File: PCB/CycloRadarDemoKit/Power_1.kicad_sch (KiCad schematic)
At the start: 33 parts, among them J401 20-16V Supply Voltage, Q401 SI2309CDS, U401 INA3221, U402 RT8259, U403 AP63205WU

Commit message: starting the mockup
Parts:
- J401: footprint (none) -> Connector_Molex:Molex_39521-1002; Mouser (none) -> 538-39521-1002
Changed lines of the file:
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@@
       (effects (font (size 1.27 1.27)))
     )
-    (property "Footprint" "" (at 64.77 113.03 0)
+    (property "Footprint" "Connector_Molex:Molex_39521-1002" (at 64.77 113.03 0)
       (effects (font (size 1.27 1.27)) hide)
     )
@@
       (effects (font (size 1.27 1.27)) hide)
     )
+    (property "Mouser" "538-39521-1002" (at 64.77 113.03 0)
+      (effects (font (size 1.27 1.27)) hide)
+    )

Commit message: layout mockup done
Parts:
- R406: symbol Device:R_Shunt -> Analog:R_Shunt
- R407: footprint Resistor_SMD:R_0805_2012Metric -> Resistor_SMD:R_1210_3225Metric; symbol Device:R_Shunt -> Analog:R_Shunt; LCSC C175747 -> C175910; Power 125mW -> 500mW
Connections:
- net at Q401.3 (S), R406.1: now also R402.2
- net at C405.1, C408.1, R406.2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: now also R403.2
- net at C404.2, L401.2, R407.1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: now also R404.2
- net at R215.1, R407.2: now also R405.2
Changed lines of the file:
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@@
   (junction (at 121.92 55.88) (diameter 0) (color 0 0 0 0)
   )
+  (junction (at 187.96 109.22) (diameter 0) (color 0 0 0 0)
+  )
   (junction (at 209.55 113.03) (diameter 0) (color 0 0 0 0)
   )
@@
   (junction (at 55.88 166.37) (diameter 0) (color 0 0 0 0)
   )
+  (junction (at 104.14 106.68) (diameter 0) (color 0 0 0 0)
+  )
+  (junction (at 101.6 110.49) (diameter 0) (color 0 0 0 0)
+  )
   (junction (at 207.01 113.03) (diameter 0) (color 0 0 0 0)
   )
@@
   (junction (at 148.59 113.03) (diameter 0) (color 0 0 0 0)
   )
+  (junction (at 193.04 109.22) (diameter 0) (color 0 0 0 0)
+  )
   (junction (at 187.96 74.93) (diameter 0) (color 0 0 0 0)
   )
@@
   (junction (at 153.67 38.1) (diameter 0) (color 0 0 0 0)
   )
+  (junction (at 111.76 110.49) (diameter 0) (color 0 0 0 0)
+  )
   (junction (at 55.88 161.29) (diameter 0) (color 0 0 0 0)
   )
   (junction (at 101.6 161.29) (diameter 0) (color 0 0 0 0)
   )
+  (junction (at 195.58 113.03) (diameter 0) (color 0 0 0 0)
+  )
   (junction (at 91.44 161.29) (diameter 0) (color 0 0 0 0)
   )
@@
   (junction (at 104.14 161.29) (diameter 0) (color 0 0 0 0)
   )
+  (junction (at 109.22 106.68) (diameter 0) (color 0 0 0 0)
+  )
   (junction (at 123.19 110.49) (diameter 0) (color 0 0 0 0)
   )
@@
   )
   (junction (at 182.88 113.03) (diameter 0) (color 0 0 0 0)
+  )
+  (junction (at 185.42 113.03) (diameter 0) (color 0 0 0 0)
   )
   (no_connect (at 149.86 43.18))
@@
     (stroke (width 0) (type default))
   )
-  (wire (pts (xy 91.44 110.49) (xy 101.6 110.49))
-    (stroke (width 0) (type default))
-  )
   (wire (pts (xy 153.67 38.1) (xy 157.48 38.1))
     (stroke (width 0) (type default))
@@
     (stroke (width 0) (type default))
   )
-  (wire (pts (xy 182.88 113.03) (xy 185.42 113.03))
-    (stroke (width 0) (type default))
-  )
   (wire (pts (xy 166.37 113.03) (xy 168.91 113.03))
     (stroke (width 0) (type default))
@@
     (stroke (width 0) (type default))
   )
+  (wire (pts (xy 195.58 113.03) (xy 195.58 109.22))
+    (stroke (width 0) (type default))
+  )
   (wire (pts (xy 156.21 110.49) (xy 153.67 110.49))
     (stroke (width 0) (type default))
@@
     (stroke (width 0) (type default))
   )
-  (wire (pts (xy 193.04 85.09) (xy 193.04 109.22))
-    (stroke (width 0) (type default))
-  )
   (wire (pts (xy 69.85 113.03) (xy 71.12 113.03))
     (stroke (width 0) (type default))
@@
   )
   (wire (pts (xy 137.16 161.29) (xy 140.97 161.29))
+    (stroke (width 0) (type default))
+  )
+  (wire (pts (xy 101.6 106.68) (xy 104.14 106.68))
     (stroke (width 0) (type default))
   )
@@
     (stroke (width 0) (type default))
   )
+  (wire (pts (xy 91.44 110.49) (xy 101.6 110.49))
+    (stroke (width 0) (type default))
+  )
   (wire (pts (xy 86.36 116.84) (xy 86.36 118.11))
     (stroke (width 0) (type default))
@@
     (stroke (width 0) (type default))
   )
+  (wire (pts (xy 111.76 106.68) (xy 111.76 110.49))
+    (stroke (width 0) (type default))
+  )
   (wire (pts (xy 209.55 110.49) (xy 209.55 113.03))
     (stroke (width 0) (type default))
   )
+  (wire (pts (xy 109.22 106.68) (xy 111.76 106.68))
+    (stroke (width 0) (type default))
+  )
   (wire (pts (xy 104.14 172.72) (xy 104.14 167.64))
     (stroke (width 0) (type default))
@@
     (stroke (width 0) (type default))
   )
+  (wire (pts (xy 193.04 85.09) (xy 193.04 109.22))
+    (stroke (width 0) (type default))
+  )
   (wire (pts (xy 124.46 45.72) (xy 119.38 45.72))
     (stroke (width 0) (type default))
   )
   (wire (pts (xy 69.85 110.49) (xy 77.47 110.49))
+    (stroke (width 0) (type default))
+  )
+  (wire (pts (xy 185.42 113.03) (xy 185.42 109.22))
+    (stroke (width 0) (type default))
+  )
+  (wire (pts (xy 195.58 109.22) (xy 193.04 109.22))
     (stroke (width 0) (type default))
   )
@@
     (stroke (width 0) (type default))
   )
+  (wire (pts (xy 182.88 113.03) (xy 185.42 113.03))
+    (stroke (width 0) (type default))
+  )
   (wire (pts (xy 123.19 110.49) (xy 123.19 127))
+    (stroke (width 0) (type default))
+  )
+  (wire (pts (xy 101.6 110.49) (xy 101.6 106.68))
     (stroke (width 0) (type default))
   )
@@
   (polyline (pts (xy 210.82 87.63) (xy 210.82 20.32))
     (stroke (width 0) (type dash))
+  )
+  (wire (pts (xy 185.42 109.22) (xy 187.96 109.22))
+    (stroke (width 0) (type default))
   )
   (wire (pts (xy 50.8 146.05) (xy 118.11 146.05))
@@
     )
   )
-  (symbol (lib_name "R_Shunt_2") (lib_id "Device:R_Shunt") (at 106.68 110.49 90) (unit 1)
+  (symbol (lib_id "Analog:R_Shunt") (at 106.68 110.49 90) (unit 1)
     (in_bom yes) (on_board yes) (dnp no)
     (property "Reference" "R406" (at 106.68 116.84 90)
@@
     )
   )
-  (symbol (lib_name "R_Shunt_1") (lib_id "Device:R_Shunt") (at 190.5 113.03 90) (unit 1)
+  (symbol (lib_name "R_Shunt_1") (lib_id "Analog:R_Shunt") (at 190.5 113.03 90) (unit 1)
     (in_bom yes) (on_board yes) (dnp no)
     (property "Reference" "R407" (at 190.5 119.38 90)
@@
       (effects (font (size 1.27 1.27)))
     )
-    (property "Footprint" "Resistor_SMD:R_0805_2012Metric" (at 190.5 114.808 90)
+    (property "Footprint" "Resistor_SMD:R_1210_3225Metric" (at 190.5 114.808 90)
       (effects (font (size 1.27 1.27)) hide)
     )
@@
       (effects (font (size 1.27 1.27)) hide)
     )
-    (property "Power" "125mW" (at 190.5 113.03 90)
-      (effects (font (size 1.27 1.27)) hide)
-    )
-    (property "LCSC" "C175747" (at 190.5 113.03 90)
-      (effects (font (size 1.27 1.27)) hide)
-    )
+    (property "Power" "500mW" (at 190.5 113.03 90)
+      (effects (font (size 1.27 1.27)) hide)
+    )
+    (property "LCSC" "C175910" (at 190.5 113.03 90)
+      (effects (font (size 1.27 1.27)) hide)
+    )

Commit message: PCB, 3Dmodel
mockup PCB version done, schcematic exported to latex, 3D model generated and exported to latex
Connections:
- net at R402.2, R406.1: no longer Q401.3 (S)
- net at C405.1, C408.1, R406.2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: no longer R403.2
- net at C404.2, L401.2, R407.1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: no longer R404.2
- net at R405.2, R407.2: no longer R215.1
- new net: Q401.3 (S), R406.1
- new net: R403.2, R406.2
- new net: R404.2, R407.1
- new net: R215.1, R407.2
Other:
- title: Safety Ride Radar Sensor -> Radar Safety Sensor
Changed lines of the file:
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@@
   (paper "A4")
   (title_block
-    (title "Safety Ride Radar Sensor")
-    (date "2023-12-19")
-    (rev "Rev.: WIP")
+    (title "Radar Safety Sensor")
+    (date "2023-12-20")
+    (rev "Rev.: 1")
     (company "ALPS Electric Czech, s.r.o.")
     (comment 1 "Designed by Martin Tavoda")
@@
   (junction (at 121.92 55.88) (diameter 0) (color 0 0 0 0)
   )
-  (junction (at 187.96 109.22) (diameter 0) (color 0 0 0 0)
-  )
   (junction (at 209.55 113.03) (diameter 0) (color 0 0 0 0)
   )
@@
   (junction (at 55.88 166.37) (diameter 0) (color 0 0 0 0)
   )
-  (junction (at 104.14 106.68) (diameter 0) (color 0 0 0 0)
-  )
-  (junction (at 101.6 110.49) (diameter 0) (color 0 0 0 0)
-  )
   (junction (at 207.01 113.03) (diameter 0) (color 0 0 0 0)
   )
@@
   (junction (at 148.59 113.03) (diameter 0) (color 0 0 0 0)
   )
-  (junction (at 193.04 109.22) (diameter 0) (color 0 0 0 0)
-  )
   (junction (at 187.96 74.93) (diameter 0) (color 0 0 0 0)
   )
@@
   (junction (at 153.67 38.1) (diameter 0) (color 0 0 0 0)
   )
-  (junction (at 111.76 110.49) (diameter 0) (color 0 0 0 0)
-  )
   (junction (at 55.88 161.29) (diameter 0) (color 0 0 0 0)
   )
   (junction (at 101.6 161.29) (diameter 0) (color 0 0 0 0)
   )
-  (junction (at 195.58 113.03) (diameter 0) (color 0 0 0 0)
-  )
   (junction (at 91.44 161.29) (diameter 0) (color 0 0 0 0)
   )
@@
   (junction (at 104.14 161.29) (diameter 0) (color 0 0 0 0)
   )
-  (junction (at 109.22 106.68) (diameter 0) (color 0 0 0 0)
-  )
   (junction (at 123.19 110.49) (diameter 0) (color 0 0 0 0)
   )
@@
   )
   (junction (at 182.88 113.03) (diameter 0) (color 0 0 0 0)
-  )
-  (junction (at 185.42 113.03) (diameter 0) (color 0 0 0 0)
   )
   (no_connect (at 149.86 43.18))
@@
     (stroke (width 0) (type default))
   )
-  (wire (pts (xy 195.58 113.03) (xy 195.58 109.22))
-    (stroke (width 0) (type default))
-  )
   (wire (pts (xy 156.21 110.49) (xy 153.67 110.49))
     (stroke (width 0) (type default))
@@
     (stroke (width 0) (type default))
   )
-  (wire (pts (xy 101.6 106.68) (xy 104.14 106.68))
-    (stroke (width 0) (type default))
-  )
   (wire (pts (xy 149.86 53.34) (xy 157.48 53.34))
     (stroke (width 0) (type default))
@@
     (stroke (width 0) (type default))
   )
-  (wire (pts (xy 111.76 106.68) (xy 111.76 110.49))
-    (stroke (width 0) (type default))
-  )
   (wire (pts (xy 209.55 110.49) (xy 209.55 113.03))
     (stroke (width 0) (type default))
   )
-  (wire (pts (xy 109.22 106.68) (xy 111.76 106.68))
-    (stroke (width 0) (type default))
-  )
   (wire (pts (xy 104.14 172.72) (xy 104.14 167.64))
     (stroke (width 0) (type default))
@@
     (stroke (width 0) (type default))
   )
-  (wire (pts (xy 185.42 113.03) (xy 185.42 109.22))
-    (stroke (width 0) (type default))
-  )
-  (wire (pts (xy 195.58 109.22) (xy 193.04 109.22))
-    (stroke (width 0) (type default))
-  )
   (wire (pts (xy 152.4 160.02) (xy 152.4 161.29))
     (stroke (width 0) (type default))
@@
     (stroke (width 0) (type default))
   )
-  (wire (pts (xy 101.6 110.49) (xy 101.6 106.68))
-    (stroke (width 0) (type default))
-  )
   (wire (pts (xy 78.74 163.83) (xy 85.09 163.83))
     (stroke (width 0) (type default))
@@
     (stroke (width 0) (type dash))
   )
-  (wire (pts (xy 185.42 109.22) (xy 187.96 109.22))
-    (stroke (width 0) (type default))
-  )
   (wire (pts (xy 50.8 146.05) (xy 118.11 146.05))

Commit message: PCB small updates, schemtatic cosmetics, SEP FINAL
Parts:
- R406, R407: symbol Analog:R_Shunt -> Device:R
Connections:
- net 20V_HS: now reaches Q401.3 (S), R406.1
- net 20V_HS: now also R402.2
- net 20V_LS: now reaches C405.1, C408.1, R406.2, U402.5 (VIN), U403.2 (EN), U403.3 (IN)
- net 20V_LS: now also R403.2
- net 12V_HS: now reaches C404.2, L401.2, R407.1, R409.1
- net 12V_HS: now also R404.2
- net 12V_LS: now reaches R215.1, R407.2
- net 12V_LS: now also R405.2
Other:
- moved on the sheet: C401, D401, D403, J401, Q401, R215, R402, R403, R404, R405, R410

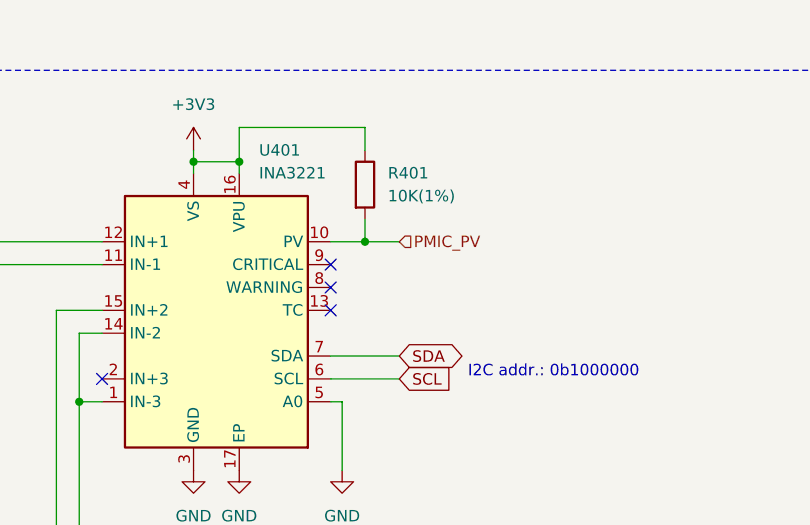
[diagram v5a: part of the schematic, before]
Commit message: All peripherals checked, changed ESP32 pinout
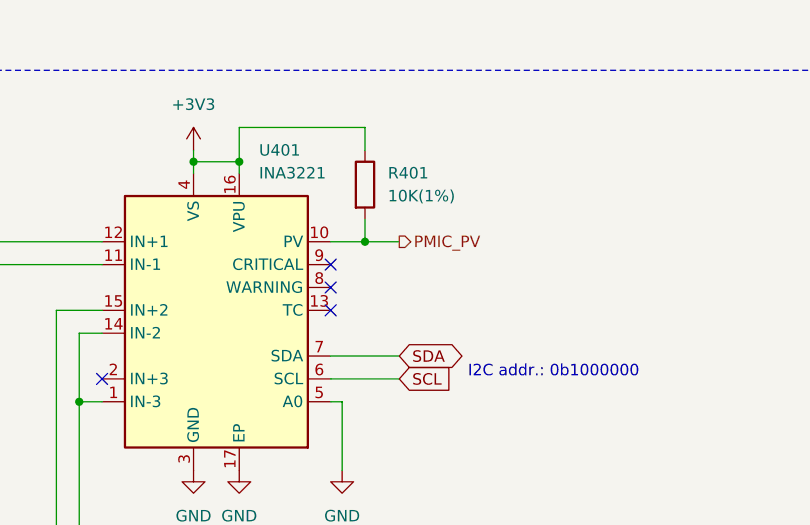
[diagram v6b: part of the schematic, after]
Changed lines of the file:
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@@
     (effects (font (size 1.27 1.27)) (justify right))
   )
-  (hierarchical_label "PMIC_PV" (shape input) (at 157.48 38.1 0) (fields_autoplaced)
+  (hierarchical_label "PMIC_PV" (shape output) (at 157.48 38.1 0) (fields_autoplaced)
     (effects (font (size 1.27 1.27)) (justify left))
   )

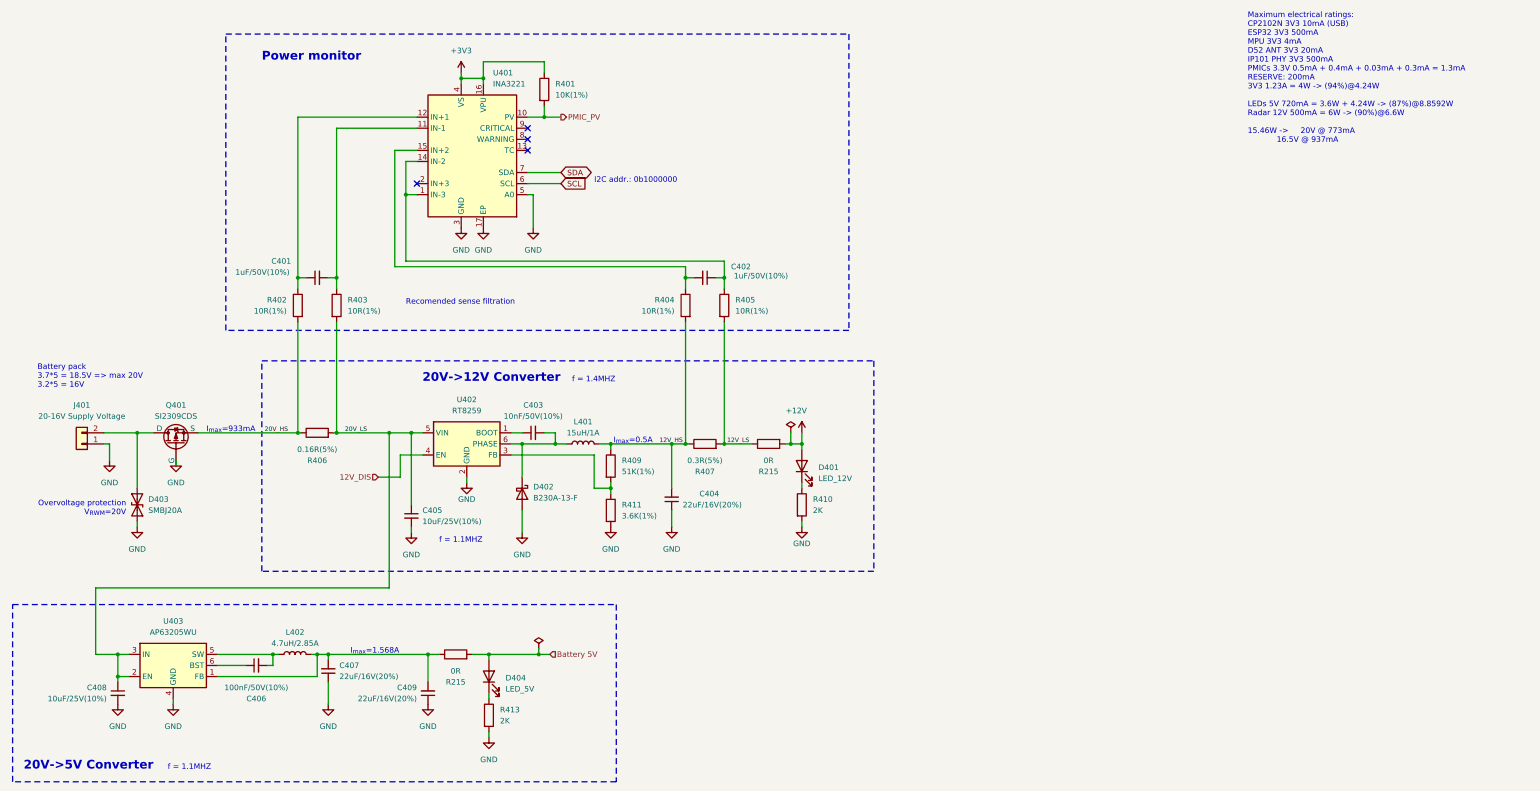
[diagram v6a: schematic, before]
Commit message: reanotated schematic, routing started
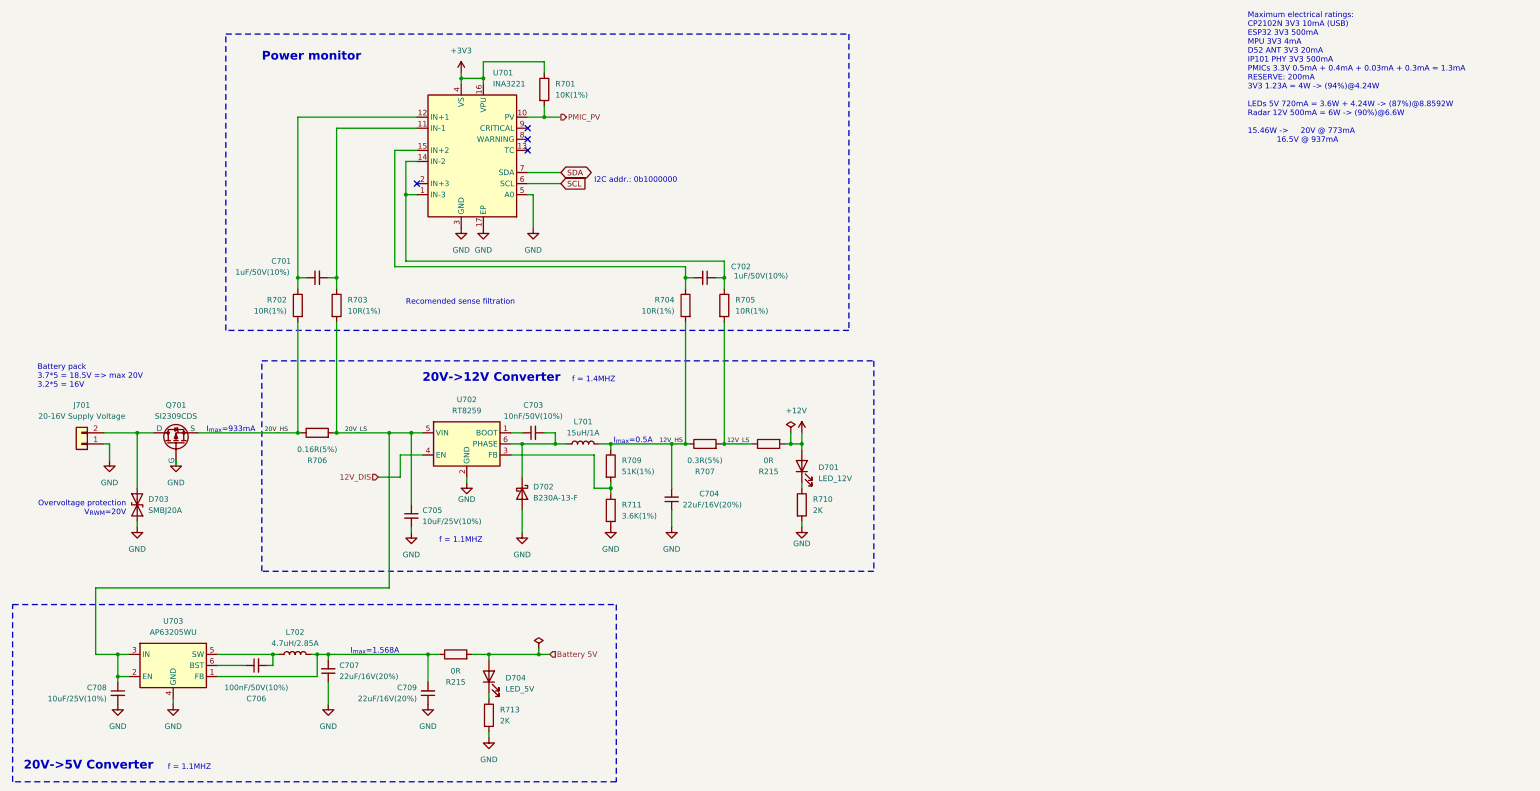
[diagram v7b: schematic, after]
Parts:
- renumbered C401 to C701, C402 to C702, C403 to C703, C404 to C704, C405 to C705, C406 to C706, C407 to C707, C408 to C708, C409 to C709, D401 to D701, D402 to D702, D403 to D703, D404 to D704, J401 to J701, L401 to L701, L402 to L702, Q401 to Q701, R401 to R701, R402 to R702, R403 to R703, R404 to R704, R405 to R705, R406 to R706, R407 to R707, R409 to R709, R410 to R710, R411 to R711, R413 to R713, U401 to U701, U402 to U702, U403 to U703

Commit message: Parts ordered on PCB, 1206->0803 10uF, 0803->0402 1uF
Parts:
- C701, C702: value 1uF/50V(10%) -> 1uF/25V(10%); footprint Capacitor_SMD:C_0603_1608Metric -> Capacitor_SMD:C_0402_1005Metric; LCSC C15849 -> C52923
- C705, C708: value 10uF/25V(10%) -> 10uF/25V(20%); footprint Capacitor_SMD:C_1206_3216Metric -> Capacitor_SMD:C_0603_1608Metric; LCSC C77090 -> C96446
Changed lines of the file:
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@@
       (effects (font (size 1.27 1.27)))
     )
-    (property "Value" "1uF/50V(10%)" (at 89.0511 73.6664 90)
-      (effects (font (size 1.27 1.27)))
-    )
-    (property "Footprint" "Capacitor_SMD:C_0603_1608Metric" (at 101.6 74.93 0)
+    (property "Value" "1uF/25V(10%)" (at 89.0511 73.6664 90)
+      (effects (font (size 1.27 1.27)))
+    )
+    (property "Footprint" "Capacitor_SMD:C_0402_1005Metric" (at 101.6 74.93 0)
       (effects (font (size 1.27 1.27)) hide)
     )
@@
       (effects (font (size 1.27 1.27)) hide)
     )
-    (property "LCSC" "C15849" (at 101.6 74.93 90)
+    (property "LCSC" "C52923" (at 101.6 74.93 90)
       (effects (font (size 1.27 1.27)) hide)
     )
@@
       (effects (font (size 1.27 1.27)) (justify left))
     )
-    (property "Value" "10uF/25V(10%)" (at 125.73 130.8163 0)
-      (effects (font (size 1.27 1.27)) (justify left))
-    )
-    (property "Footprint" "Capacitor_SMD:C_1206_3216Metric" (at 123.19 129.54 0)
+    (property "Value" "10uF/25V(20%)" (at 125.73 130.8163 0)
+      (effects (font (size 1.27 1.27)) (justify left))
+    )
+    (property "Footprint" "Capacitor_SMD:C_0603_1608Metric" (at 123.19 129.54 0)
       (effects (font (size 1.27 1.27)) hide)
     )
@@
       (effects (font (size 1.27 1.27)) hide)
     )
-    (property "LCSC" "C77090" (at 123.19 129.54 0)
+    (property "LCSC" "C96446" (at 123.19 129.54 0)
       (effects (font (size 1.27 1.27)) hide)
     )
@@
       (effects (font (size 1.27 1.27)))
     )
-    (property "Value" "1uF/50V(10%)" (at 203.3476 74.4979 90)
-      (effects (font (size 1.27 1.27)))
-    )
-    (property "Footprint" "Capacitor_SMD:C_0603_1608Metric" (at 190.5 74.93 0)
+    (property "Value" "1uF/25V(10%)" (at 203.3476 74.4979 90)
+      (effects (font (size 1.27 1.27)))
+    )
+    (property "Footprint" "Capacitor_SMD:C_0402_1005Metric" (at 190.5 74.93 0)
       (effects (font (size 1.27 1.27)) hide)
     )
@@
       (effects (font (size 1.27 1.27)) hide)
     )
-    (property "LCSC" "C15849" (at 190.5 74.93 0)
+    (property "LCSC" "C52923" (at 190.5 74.93 0)
       (effects (font (size 1.27 1.27)) hide)
     )
@@
       (effects (font (size 1.27 1.27)) (justify left))
     )
-    (property "Value" "10uF/25V(10%)" (at 53.34 171.4563 0)
-      (effects (font (size 1.27 1.27)) (justify left))
-    )
-    (property "Footprint" "Capacitor_SMD:C_1206_3216Metric" (at 55.88 170.18 0)
+    (property "Value" "10uF/25V(20%)" (at 53.34 171.4563 0)
+      (effects (font (size 1.27 1.27)) (justify left))
+    )
+    (property "Footprint" "Capacitor_SMD:C_0603_1608Metric" (at 55.88 170.18 0)
       (effects (font (size 1.27 1.27)) hide)
     )
@@
       (effects (font (size 1.27 1.27)) hide)
     )
-    (property "LCSC" "C77090" (at 55.88 170.18 0)
-      (effects (font (size 1.27 1.27)) hide)
-    )
+    (property "LCSC" "C96446" (at 55.88 170.18 0)
+      (effects (font (size 1.27 1.27)) hide)
+    )
